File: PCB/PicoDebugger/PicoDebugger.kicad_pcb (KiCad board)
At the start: 2 copper layers, 116.7 x 55.7 mm, 10 parts, among them J1 External_Connections, J2 SWD, SW1 UART, SW2 Reset_Target

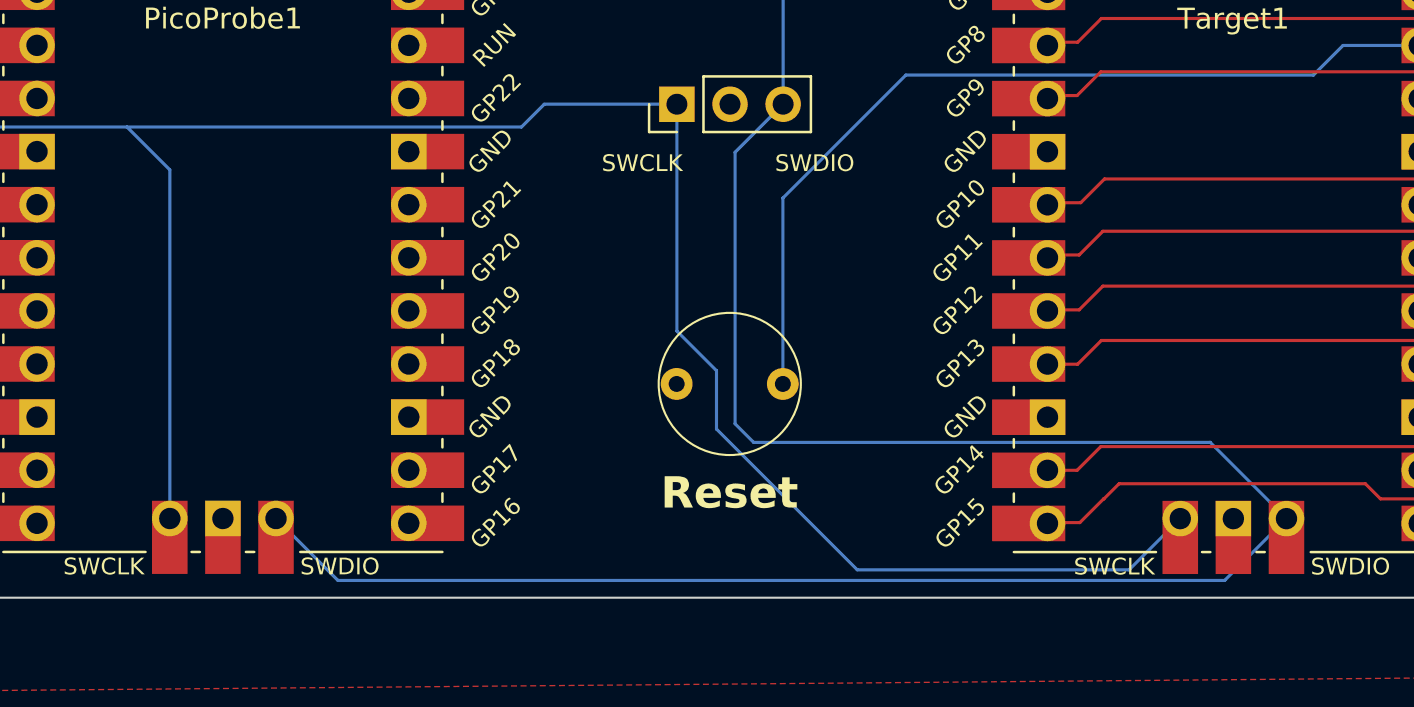
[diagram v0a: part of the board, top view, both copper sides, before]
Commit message: Updated design, added PicoW version
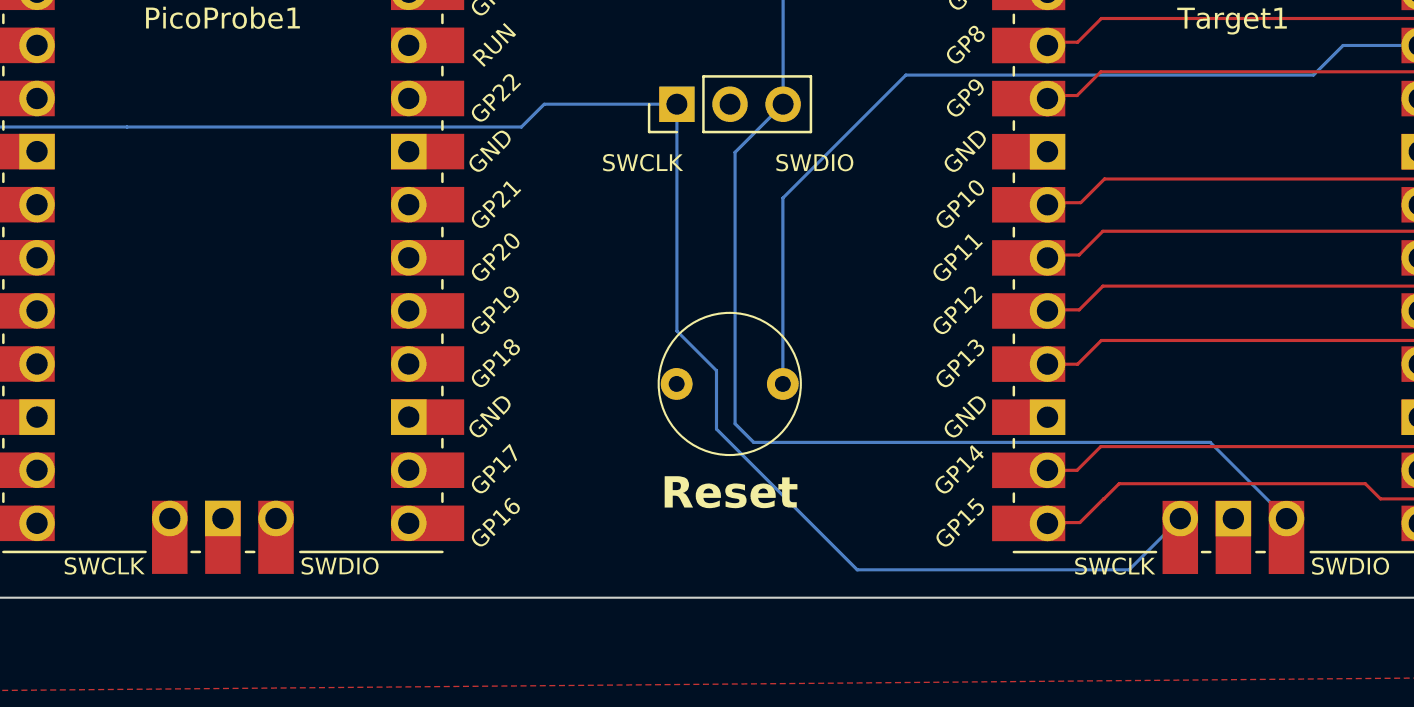
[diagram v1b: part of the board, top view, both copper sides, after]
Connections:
- PicoProbe1 pad 41: /SWCLK -> unconnected-(PicoProbe1-SWCLK-Pad41)
- PicoProbe1 pad 43: /SWDIO -> unconnected-(PicoProbe1-SWDIO-Pad43)
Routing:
- net /SWDIO: track 142.4 -> 91.6 mm
- net /SWCLK: track 125.8 -> 106.3 mm
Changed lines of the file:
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@@
   (net 64 "/TT_GPIO15")
   (net 65 "/TT_GPIO16")
+  (net 66 "unconnected-(PicoProbe1-SWCLK-Pad41)")
+  (net 67 "unconnected-(PicoProbe1-SWDIO-Pad43)")
   (footprint "MountingHole:MountingHole_2.5mm" (layer "F.Cu")
     (at 50 72)
     (descr "Mounting Hole 2.5mm, no annular")
     (tags "mounting hole 2.5mm no annular")
-    (property "Sheetfile" "PicoprobeTester.kicad_sch")
+    (property "Sheetfile" "PicoDebugger.kicad_sch")
     (property "Sheetname" "")
     (property "ki_description" "Mounting Hole without connection")
@@
     (descr "Mounting Hole 2.5mm, no annular")
     (tags "mounting hole 2.5mm no annular")
-    (property "Sheetfile" "PicoprobeTester.kicad_sch")
+    (property "Sheetfile" "PicoDebugger.kicad_sch")
     (property "Sheetname" "")
     (property "ki_description" "Mounting Hole without connection")
@@
     (descr "Through hole straight pin header, 2x20, 2.54mm pitch, double rows")
     (tags "Through hole pin header THT 2x20 2.54mm double row")
-    (property "Sheetfile" "PicoprobeTester.kicad_sch")
+    (property "Sheetfile" "PicoDebugger.kicad_sch")
     (property "Sheetname" "")
     (attr through_hole)
@@
     (descr "Mounting Hole 2.5mm, no annular")
     (tags "mounting hole 2.5mm no annular")
-    (property "Sheetfile" "PicoprobeTester.kicad_sch")
+    (property "Sheetfile" "PicoDebugger.kicad_sch")
     (property "Sheetname" "")
     (property "ki_description" "Mounting Hole without connection")
@@
     (descr "Through hole straight pin header, 1x03, 2.54mm pitch, single row")
     (tags "Through hole pin header THT 1x03 2.54mm single row")
-    (property "Sheetfile" "PicoprobeTester.kicad_sch")
+    (property "Sheetfile" "PicoDebugger.kicad_sch")
     (property "Sheetname" "")
     (property "ki_description" "Generic connector, single row, 01x03, script generated (kicad-library-utils/schlib/autogen/connector/)")
@@
     (descr "Mounting Hole 2.5mm, no annular")
     (tags "mounting hole 2.5mm no annular")
-    (property "Sheetfile" "PicoprobeTester.kicad_sch")
+    (property "Sheetfile" "PicoDebugger.kicad_sch")
     (property "Sheetname" "")
     (property "ki_description" "Mounting Hole without connection")
@@
   (footprint "ThePCSite:Alps_SKRGAFD010" (layer "F.Cu")
     (at 93.853 114.554)
-    (property "Sheetfile" "PicoprobeTester.kicad_sch")
+    (property "Sheetfile" "PicoDebugger.kicad_sch")
     (property "Sheetname" "")
     (property "ki_description" "Push button switch, generic, two pins")
@@
     (descr "Through hole straight pin header, 2x20, 2.54mm pitch, double rows")
     (tags "Through hole pin header THT 2x20 2.54mm double row")
-    (property "Sheetfile" "PicoprobeTester.kicad_sch")
+    (property "Sheetfile" "PicoDebugger.kicad_sch")
     (property "Sheetname" "")
     (property "ki_description" "Generic connector, double row, 02x20, odd/even pin numbering scheme (row 1 odd numbers, row 2 even numbers), script generated (kicad-library-utils/schlib/autogen/connector/)")
@@
     (descr "2x-dip-switch SPST , Slide, row spacing 7.62 mm (300 mils), body size 9.78x7.26mm (see e.g. https://www.ctscorp.com/wp-content/uploads/206-208.pdf)")
     (tags "DIP Switch SPST Slide 7.62mm 300mil")
-    (property "Sheetfile" "PicoprobeTester.kicad_sch")
+    (property "Sheetfile" "PicoDebugger.kicad_sch")
     (property "Sheetname" "")
     (property "ki_description" "2x DIP Switch, Single Pole Single Throw (SPST) switch, small symbol")
@@
     (descr "Through hole straight pin header, 2x20, 2.54mm pitch, double rows")
     (tags "Through hole pin header THT 2x20 2.54mm double row")
-    (property "Sheetfile" "PicoprobeTester.kicad_sch")
+    (property "Sheetfile" "PicoDebugger.kicad_sch")
     (property "Sheetname" "")
     (attr through_hole)
@@
       (net 40 "/VBus") (pinfunction "VBUS") (pintype "unspecified"))
     (pad "41" thru_hole oval (at -2.54 23.9) (size 1.7 1.7) (drill 1.02) (layers "*.Cu" "*.Mask")
-      (net 10 "/SWCLK") (pinfunction "SWCLK") (pintype "input"))
+      (net 66 "unconnected-(PicoProbe1-SWCLK-Pad41)") (pinfunction "SWCLK") (pintype "input+no_connect"))
     (pad "41" smd rect (at -2.54 23.9 90) (size 3.5 1.7) (drill (offset -0.9 0)) (layers "F.Cu" "F.Mask")
-      (net 10 "/SWCLK") (pinfunction "SWCLK") (pintype "input"))
+      (net 66 "unconnected-(PicoProbe1-SWCLK-Pad41)") (pinfunction "SWCLK") (pintype "input+no_connect"))
     (pad "42" thru_hole rect (at 0 23.9) (size 1.7 1.7) (drill 1.02) (layers "*.Cu" "*.Mask")
       (net 41 "unconnected-(PicoProbe1-GND-Pad42)") (pinfunction "GND") (pintype "power_in"))
@@
       (net 41 "unconnected-(PicoProbe1-GND-Pad42)") (pinfunction "GND") (pintype "power_in"))
     (pad "43" thru_hole oval (at 2.54 23.9) (size 1.7 1.7) (drill 1.02) (layers "*.Cu" "*.Mask")
-      (net 11 "/SWDIO") (pinfunction "SWDIO") (pintype "bidirectional"))
+      (net 67 "unconnected-(PicoProbe1-SWDIO-Pad43)") (pinfunction "SWDIO") (pintype "bidirectional+no_connect"))
     (pad "43" smd rect (at 2.54 23.9 90) (size 3.5 1.7) (drill (offset -0.9 0)) (layers "F.Cu" "F.Mask")
-      (net 11 "/SWDIO") (pinfunction "SWDIO") (pintype "bidirectional"))
+      (net 67 "unconnected-(PicoProbe1-SWDIO-Pad43)") (pinfunction "SWDIO") (pintype "bidirectional+no_connect"))
   )
   (gr_arc (start 49.997577 124.777423) (mid 48 123.95) (end 47.172577 121.952423)
@@
   (segment (start 54.229 100.965) (end 55.529 102.265) (width 0.15) (layer "B.Cu") (net 10))
   (segment (start 91.325 101.175) (end 91.325 112.026) (width 0.15) (layer "B.Cu") (net 10))
-  (segment (start 67.07 104.311) (end 65.024 102.265) (width 0.15) (layer "B.Cu") (net 10))
   (segment (start 55.945 80.58) (end 54.229 82.296) (width 0.15) (layer "B.Cu") (net 10))
-  (segment (start 67.07 120.99) (end 67.07 104.311) (width 0.15) (layer "B.Cu") (net 10))
   (segment (start 83.89 102.265) (end 84.98 101.175) (width 0.15) (layer "B.Cu") (net 10))
   (segment (start 60.72 80.58) (end 55.945 80.58) (width 0.15) (layer "B.Cu") (net 10))
@@
   (segment (start 94.107 103.473) (end 94.107 116.459) (width 0.15) (layer "B.Cu") (net 11))
   (segment (start 116.833 117.348) (end 120.48 120.995) (width 0.15) (layer "B.Cu") (net 11))
-  (segment (start 117.523 123.952) (end 75.112 123.952) (width 0.15) (layer "B.Cu") (net 11))
-  (segment (start 75.112 123.952) (end 72.15 120.99) (width 0.15) (layer "B.Cu") (net 11))
   (segment (start 96.405 101.175) (end 94.107 103.473) (width 0.15) (layer "B.Cu") (net 11))
   (segment (start 116.833 117.348) (end 94.996 117.348) (width 0.15) (layer "B.Cu") (net 11))
-  (segment (start 120.48 120.995) (end 117.523 123.952) (width 0.15) (layer "B.Cu") (net 11))
   (segment (start 89.4795 86.868) (end 90.8075 85.54) (width 0.15) (layer "F.Cu") (net 12))
   (segment (start 65.151 86.868) (end 89.4795 86.868) (width 0.15) (layer "F.Cu") (net 12))
